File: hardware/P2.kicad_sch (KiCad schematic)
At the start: 17 parts, among them SW1 SW_DPST_x2, SW2 SW_DPST_x2, U1 Pico, U7 AP63203WU

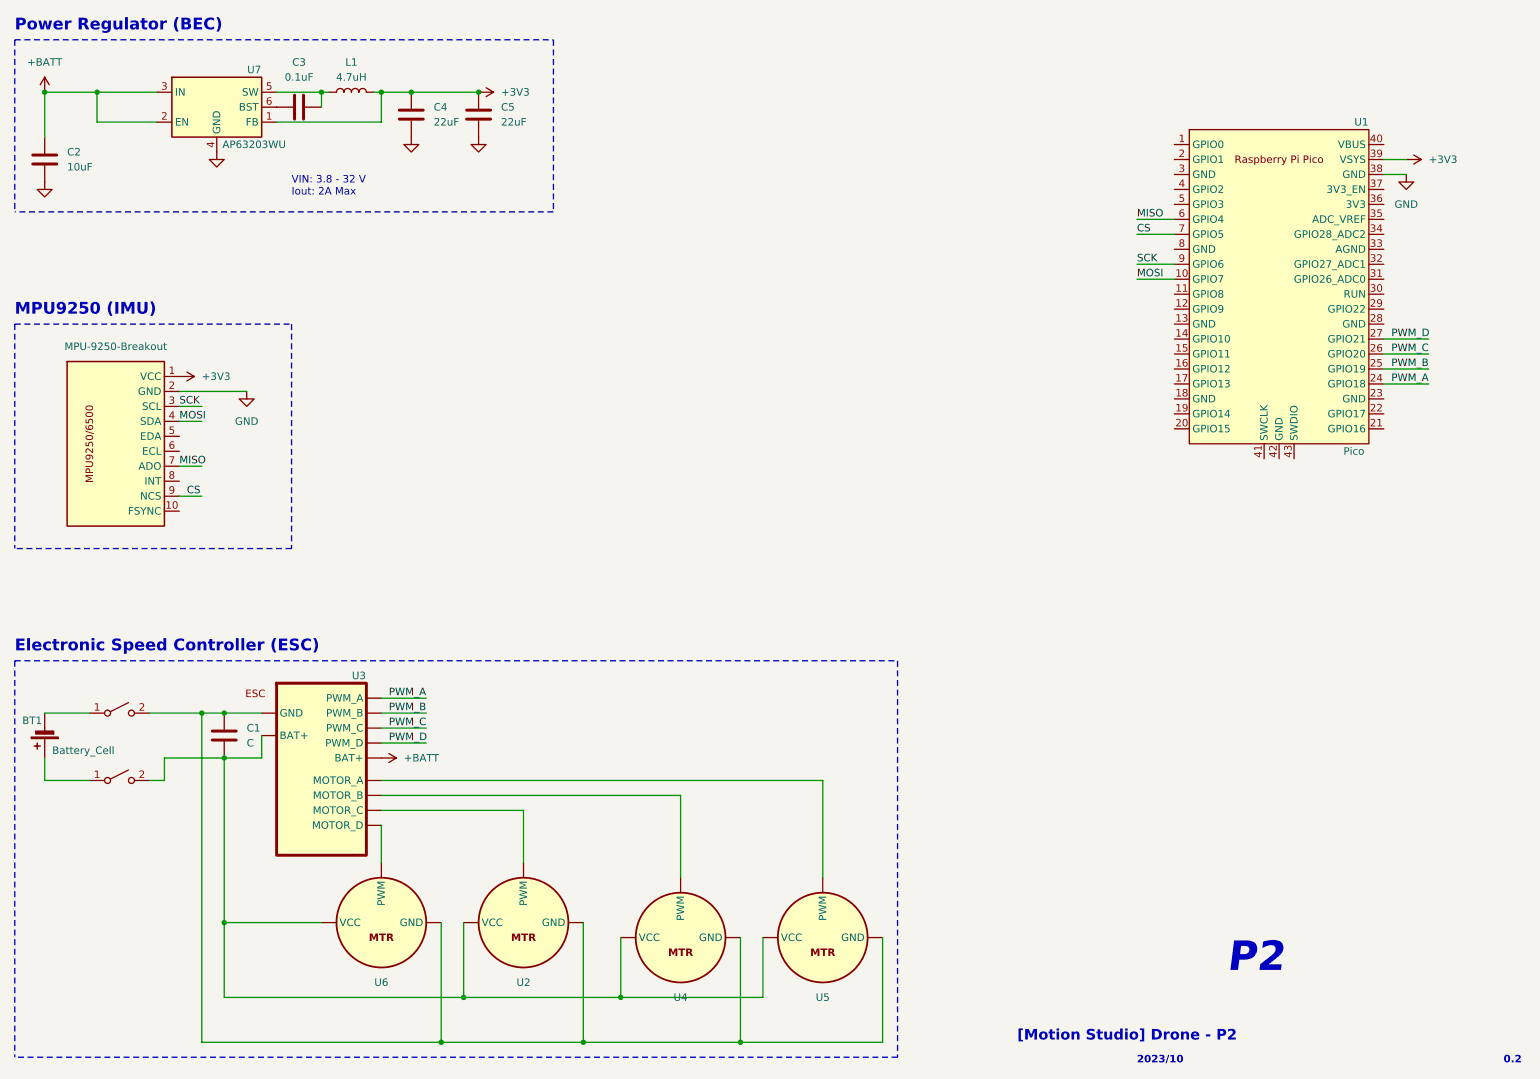
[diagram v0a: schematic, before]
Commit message: add radio
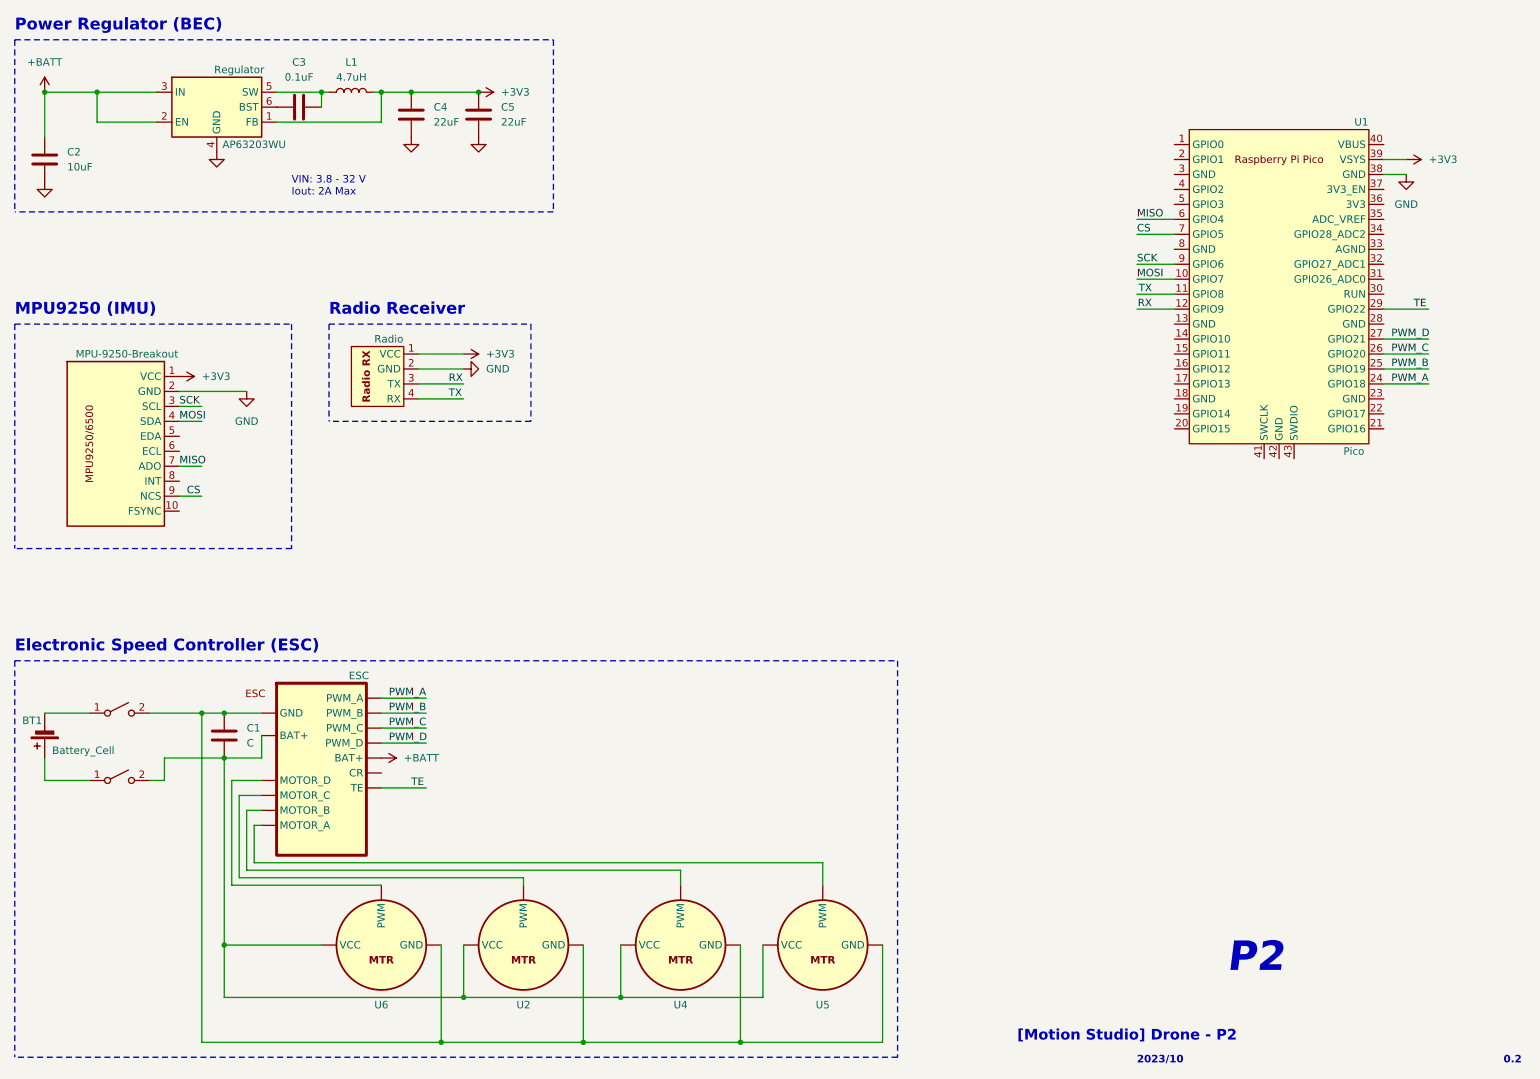
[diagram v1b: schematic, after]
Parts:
- added Radio: ~, symbol Parts:HappyModelRadio_Recevier
- renumbered U3 to ESC, U7 to Regulator
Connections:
- net +3V3: now also Radio.1 (VCC)
- net GND: now also Radio.2 (GND)
- net TX: now reaches U1.11 (GPIO8)
- net TX: now also Radio.4 (RX)
- net RX: now reaches U1.12 (GPIO9)
- net RX: now also Radio.3 (TX)
- net TE: now reaches U1.29 (GPIO22)
- net TE: now also ESC. (TE)
- new net: C1.1, ESC. (TE), SW1.2 (B), U2. (VCC), U4. (VCC), U5. (VCC), U6. (VCC)
- new net: C1.2, ESC. (TE), SW2.2 (B), U2. (VCC), U4. (VCC), U5. (VCC), U6. (VCC)
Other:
- note added: "Radio Receiver"
- moved on the sheet: U2, U4, U5, U6

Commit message: pre-pcb design
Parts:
- removed SW1, SW2: SW_DPST_x2, symbol Switch:SW_DPST_x2
- added TP1: TX0, TestPoint:TestPoint_Pad_D2.0mm, symbol Connector:TestPoint
- added TP2: TX1, TestPoint:TestPoint_Pad_D2.0mm, symbol Connector:TestPoint
- added TP3: GND, TestPoint:TestPoint_Pad_D2.0mm, symbol Connector:TestPoint
- C2: footprint (none) -> Capacitor_SMD:C_0603_1608Metric
- C3: footprint (none) -> Capacitor_SMD:C_0402_1005Metric
- C4, C5: footprint (none) -> Capacitor_SMD:C_0805_2012Metric
- ESC1: renamed from ESC; footprint (none) -> footprint:ESC
- Radio1: renamed from Radio; footprint (none) -> footprint:Radio
- U1: footprint RPi_Pico:RPi_Pico_SMD_TH -> MCU_RaspberryPi_and_Boards:RPi_Pico_SMD_TH
- renumbered MPU-9250-Breakout to MPU-9250-Breakout1, Regulator to Regulator1
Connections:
- net +BATT: now also ESC1.5 (BAT+); no longer ESC1. (TE)
- net GND: now also U1.3 (GND), TP3.1; no longer U1.38 (GND)
- net PWM_A: now also ESC1.1 (PWM_A); no longer ESC1. (TE)
- net PWM_B: now also ESC1.2 (PWM_B); no longer ESC1. (TE)
- net PWM_C: now also ESC1.3 (PWM_C); no longer ESC1. (TE)
- net PWM_D: now also ESC1.4 (PWM_D); no longer ESC1. (TE)
- net TE: now also ESC1.6 (TE); no longer ESC1. (TE)
- net at BT1.1 (+): now also C1.2, ESC1. (MOTOR_D), U2. (VCC), U4. (VCC), U5. (VCC), U6. (VCC)
- net at BT1.2 (-): now also C1.1, ESC1. (MOTOR_D), U2. (VCC), U4. (VCC), U5. (VCC), U6. (VCC)
- net at ESC1. (MOTOR_D): now also U5. (VCC)
- net at U1.1 (GPIO0): now also TP1.1
- net at U1.2 (GPIO1): now also TP2.1
- no-connect marks 0 -> 33
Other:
- note added: "Microcontroller (Pico)"
- moved on the sheet: U1

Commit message: pcb done
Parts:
- added H1, H2, H3, H4: MountingHole, MountingHole:MountingHole_2.2mm_M2, symbol Mechanical:MountingHole
- L1: footprint (none) -> Inductor_SMD:L_Abracon_ASPI-4030S
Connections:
- net GND: now also ESC1.7 (GND)
- net at ESC1. (MOTOR_D): now also U5. (VCC)
- new net: BT1.2 (-), C1.1, ESC1. (MOTOR_D), U2. (VCC), U4. (VCC), U5. (VCC), U6. (VCC)
- new net: BT1.1 (+), C1.2, ESC1. (MOTOR_D), U2. (VCC), U4. (VCC), U5. (VCC), U6. (VCC)
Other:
- note added: "Mounting Holes (M2)"

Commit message: change pkg
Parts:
- C2: footprint Capacitor_SMD:C_0603_1608Metric -> Capacitor_SMD:C_0805_2012Metric
- C3: footprint Capacitor_SMD:C_0402_1005Metric -> Capacitor_SMD:C_0805_2012Metric
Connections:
- net at ESC1. (MOTOR_D): now also U5. (VCC)
- new net: BT1.2 (-), C1.1, ESC1. (MOTOR_D), U2. (VCC), U4. (VCC), U5. (VCC), U6. (VCC)
- new net: BT1.1 (+), C1.2, ESC1. (MOTOR_D), U2. (VCC), U4. (VCC), U5. (VCC), U6. (VCC)
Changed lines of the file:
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@@
       (effects (font (size 1.27 1.27)) (justify left))
     )
-    (property "Footprint" "Capacitor_SMD:C_0603_1608Metric" (at 23.8252 44.45 0)
+    (property "Footprint" "Capacitor_SMD:C_0805_2012Metric" (at 23.8252 44.45 0)
       (effects (font (size 1.27 1.27)) hide)
     )
@@
       (effects (font (size 1.27 1.27)))
     )
-    (property "Footprint" "Capacitor_SMD:C_0402_1005Metric" (at 69.85 30.7848 0)
-      (effects (font (size 1.27 1.27)) hide)
-    )
+    (property "Footprint" "Capacitor_SMD:C_0805_2012Metric" (at 69.85 30.7848 0)
+      (effects (font (size 1.27 1.27)) hide)
+    )

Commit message: update svg
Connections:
- net at ESC1. (MOTOR_D): now also U5. (VCC)
- new net: BT1.2 (-), C1.1, ESC1. (MOTOR_D), U2. (VCC), U4. (VCC), U5. (VCC), U6. (VCC)
- new net: BT1.1 (+), C1.2, ESC1. (MOTOR_D), U2. (VCC), U4. (VCC), U5. (VCC), U6. (VCC)
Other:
- note added: "1.0"
- note added: "2024/2/25"
- note removed: "0.2"
- note removed: "2023/10"
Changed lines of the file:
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@@
     (effects (font (size 5 5) (thickness 1) bold italic) (justify left bottom))
   )
-  (text "2023/10" (at 208.28 194.31 0)
+  (text "2024/2/25" (at 208.28 194.31 0)
     (effects (font (size 1.27 1.27) bold) (justify left bottom))
   )
@@
     (effects (font (face "KiCad Font") (size 1.8 1.8) (thickness 0.254) bold) (justify left bottom))
   )
-  (text "0.2" (at 270.51 194.31 0)
+  (text "1.0" (at 270.51 194.31 0)
     (effects (font (size 1.27 1.27) bold) (justify left bottom))
   )

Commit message: builder scripter
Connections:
- net at ESC1. (MOTOR_D): now also U5. (VCC)
- new net: BT1.2 (-), C1.1, ESC1. (MOTOR_D), U2. (VCC), U4. (VCC), U5. (VCC), U6. (VCC)
- new net: BT1.1 (+), C1.2, ESC1. (MOTOR_D), U2. (VCC), U4. (VCC), U5. (VCC), U6. (VCC)
